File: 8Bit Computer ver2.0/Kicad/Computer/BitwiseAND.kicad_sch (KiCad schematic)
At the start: 5 parts, among them IC30 SN74LVC1G14DBVR, IC35 SN74AHC08DR, IC38 SN74AHC08DR, IC40 SN74ABT574ADWR, IC62 SN74AHC74DR

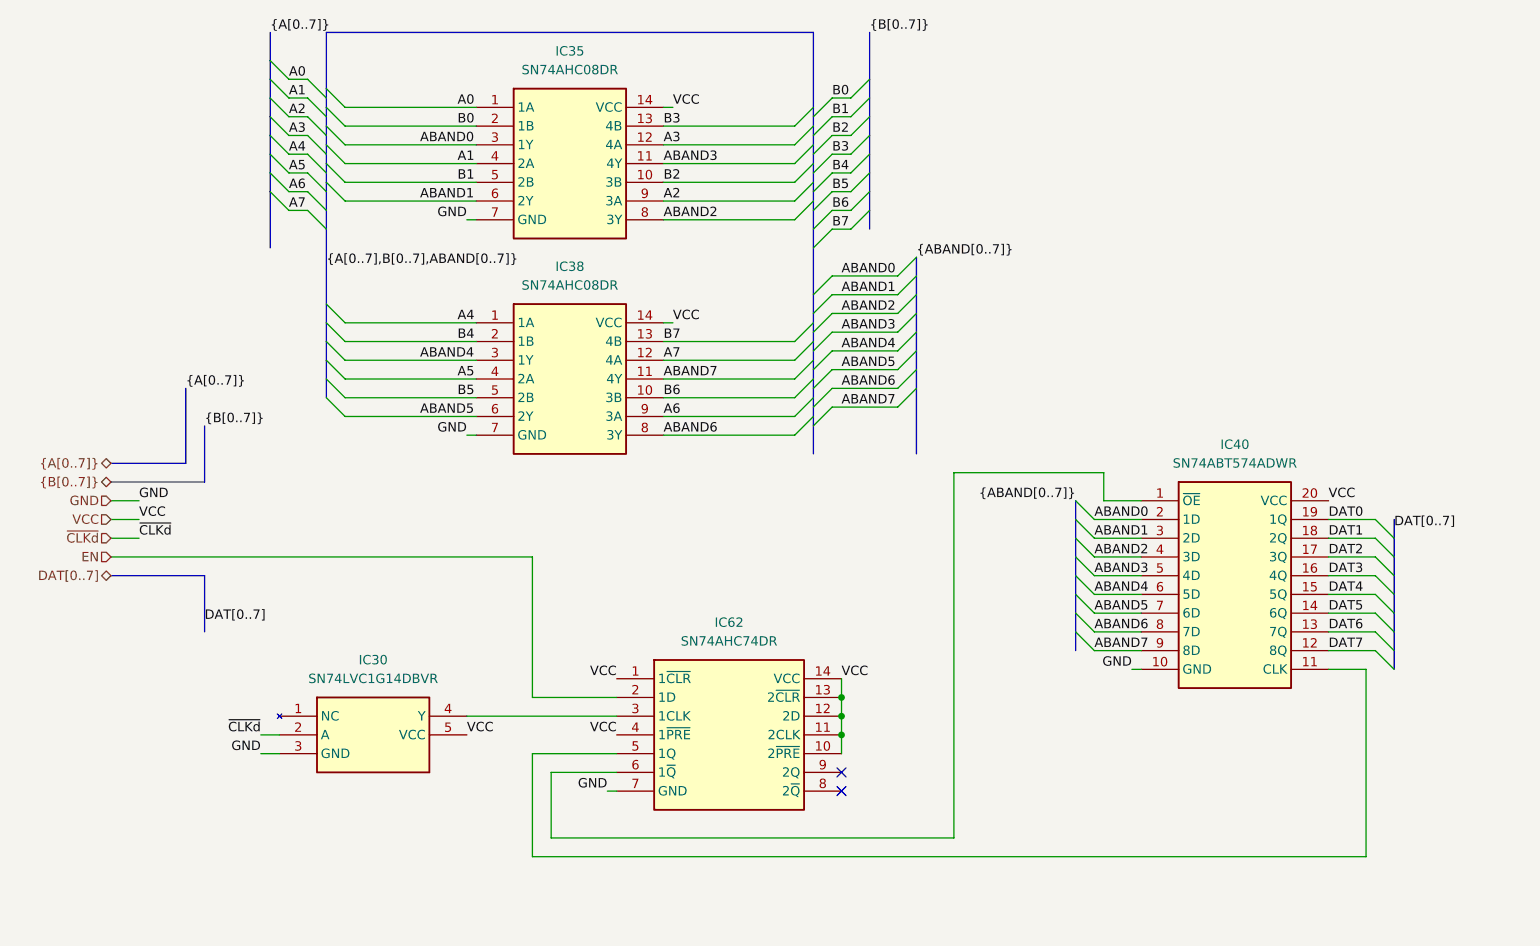
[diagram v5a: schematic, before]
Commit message: Kicad SCH/PCB
Kicad SCH/PCB:
changed the References in SCH
began with INOUTPUT module nearly done
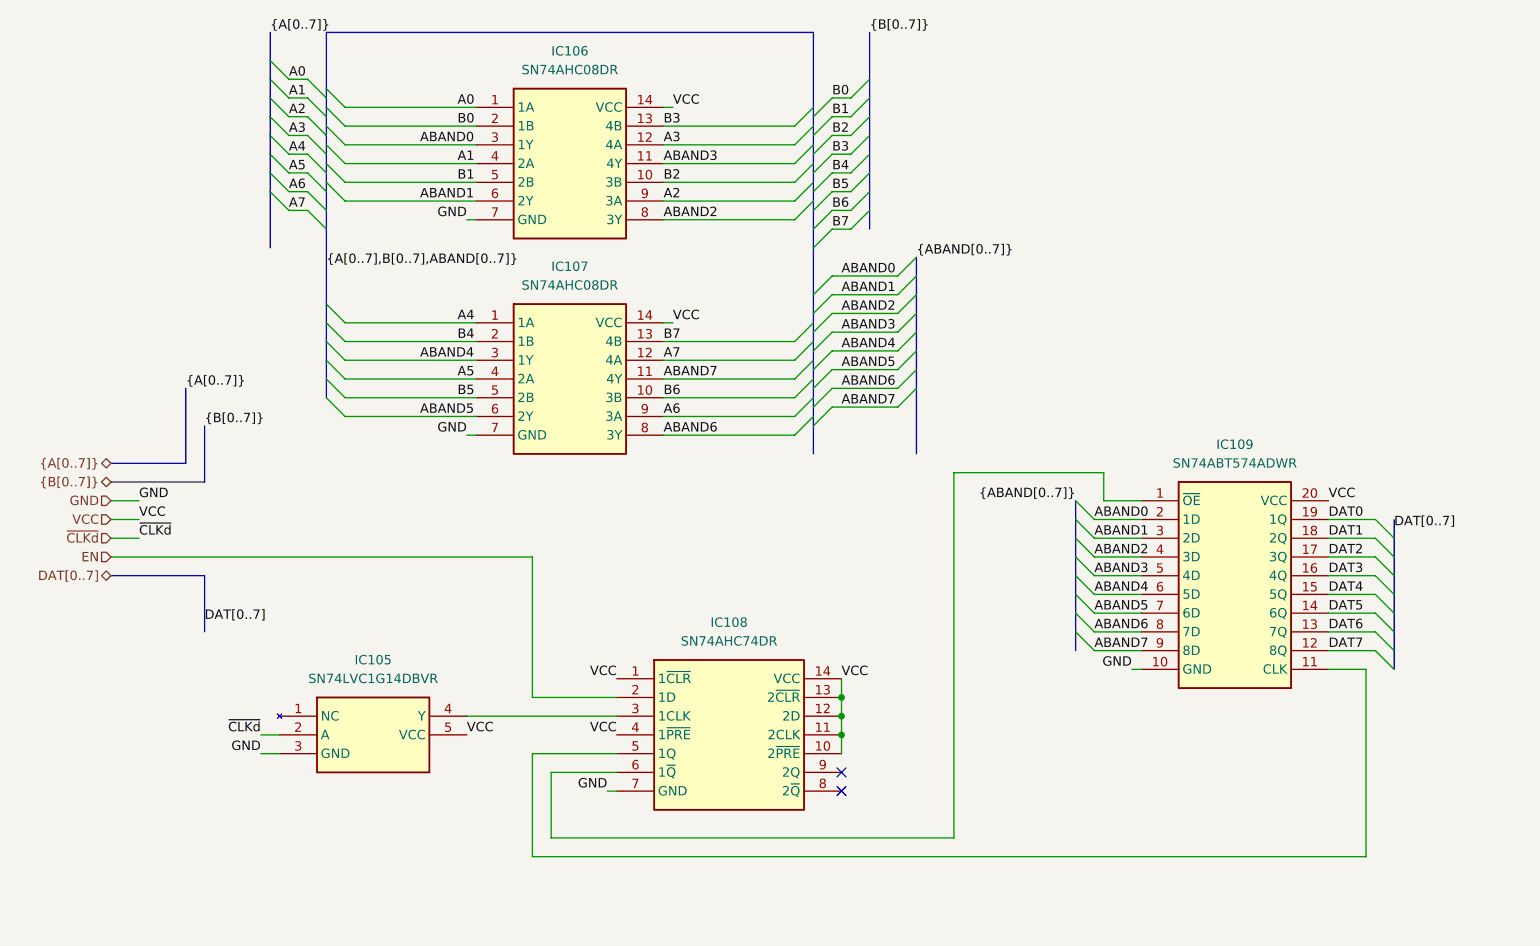
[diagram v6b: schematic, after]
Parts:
- renumbered IC30 to IC105, IC35 to IC106, IC38 to IC107, IC62 to IC108, IC40 to IC109
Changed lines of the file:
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@@
 		(dnp no)
 		(fields_autoplaced yes)
-		(property "Reference" "IC38"
+		(property "Reference" "IC107"
 			(at 111.76 64.77 0)
 			(effects
@@
 			(project "Computer"
 				(path "/1196a00e-6878-4d6d-82b7-9e052dfe7c14/c4d8b530-1c6d-45af-88d2-7dc1d4321a34/88d9deac-8ee4-4e62-9612-525be97c3130"
-					(reference "IC38")
+					(reference "IC107")
 					(unit 1)
 				)
@@
 		(dnp no)
 		(fields_autoplaced yes)
-		(property "Reference" "IC62"
+		(property "Reference" "IC108"
 			(at 133.35 113.03 0)
 			(effects
@@
 			(project "Computer"
 				(path "/1196a00e-6878-4d6d-82b7-9e052dfe7c14/c4d8b530-1c6d-45af-88d2-7dc1d4321a34/88d9deac-8ee4-4e62-9612-525be97c3130"
-					(reference "IC62")
+					(reference "IC108")
 					(unit 1)
 				)
@@
 		(dnp no)
 		(fields_autoplaced yes)
-		(property "Reference" "IC30"
+		(property "Reference" "IC105"
 			(at 85.09 118.11 0)
 			(effects
@@
 			(project "Computer"
 				(path "/1196a00e-6878-4d6d-82b7-9e052dfe7c14/c4d8b530-1c6d-45af-88d2-7dc1d4321a34/88d9deac-8ee4-4e62-9612-525be97c3130"
-					(reference "IC30")
+					(reference "IC105")
 					(unit 1)
 				)
@@
 		(dnp no)
 		(fields_autoplaced yes)
-		(property "Reference" "IC40"
+		(property "Reference" "IC109"
 			(at 201.93 88.9 0)
 			(effects
@@
 			(project "Computer"
 				(path "/1196a00e-6878-4d6d-82b7-9e052dfe7c14/c4d8b530-1c6d-45af-88d2-7dc1d4321a34/88d9deac-8ee4-4e62-9612-525be97c3130"
-					(reference "IC40")
+					(reference "IC109")
 					(unit 1)
 				)
@@
 		(dnp no)
 		(fields_autoplaced yes)
-		(property "Reference" "IC35"
+		(property "Reference" "IC106"
 			(at 111.76 35.56 0)
 			(effects
@@
 			(project "Computer"
 				(path "/1196a00e-6878-4d6d-82b7-9e052dfe7c14/c4d8b530-1c6d-45af-88d2-7dc1d4321a34/88d9deac-8ee4-4e62-9612-525be97c3130"
-					(reference "IC35")
+					(reference "IC106")
 					(unit 1)
 				)

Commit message: changed page numbers, compressed ROOT file from A1 to A4
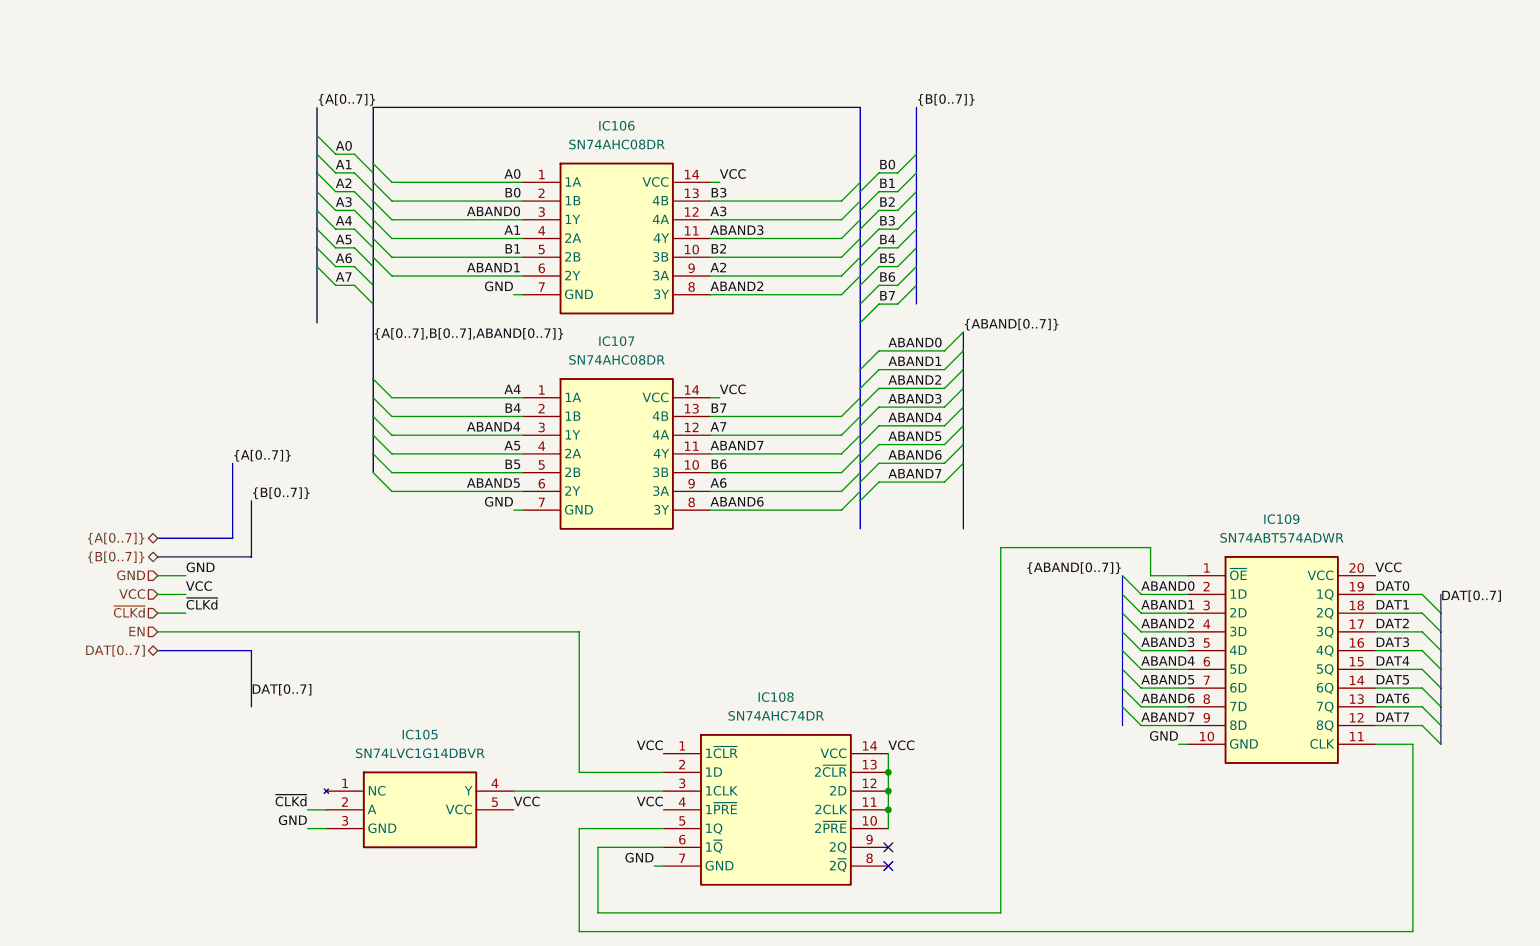
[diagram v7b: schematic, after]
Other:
- moved on the sheet: IC107, IC108, IC109

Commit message: changed page numbers, every schematic is now A4
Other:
- title: (none) -> ${SHEETNAME}
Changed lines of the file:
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@@
 	(generator_version "9.0")
 	(paper "A4")
+	(title_block
+		(title "${SHEETNAME}")
+		(date "2026-03-21")
+		(rev "2.7")
+	)
 	(junction
 		(at 154.94 138.43)
